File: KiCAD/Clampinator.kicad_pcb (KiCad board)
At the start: 4 copper layers, 200 x 130 mm, 194 parts, among them J1 Power, J10 Conn_01x04, J11 Conn_01x04, J12 FDCAN_1, J13 FDCAN_2, J14 10k NTC, J15 10k NTC, J16 EN_NTC_B, J17 EN_NTC_A, J18 FAN, J19 FAN, J20 VP0265840000G, J23 VP0265840000G, J24 VP0265840000G, J25 +5V INJ, J5 Debug Header, J6 Conn_01x04, J7 Conn_01x04, J8 Conn_01x04, J9 Conn_01x04, Q1 TK100E10N1,S1X, Q10 AO3400A, Q2 TK100E10N1,S1X, Q3 TK100E10N1,S1X, Q4 TK100E10N1,S1X, Q5 TK100E10N1,S1X, Q6 AO3400A, Q7 AO3400A, Q8 AO3400A, Q9 MMBT3904-C20526, SW1 PTS810SJM250SMTRLFS, SW2 PTS810SJM250SMTRLFS, SW3 PTS810SJM250SMTRLFS, SW4 PTS810SJM250SMTRLFS, SW5 SMQS-02R-TP, SW6 EG1847-ND, SW7 GPI-154-3013, U1 STM32H573RIT6, U10 LM74810QDRRRQ1, U12 TPS7A2033DQNR, U13 VOS618A-3T, U14 LM5163DDAR, U2 TL432BQDBZR, U3 EG2131, U4 UCC33420RAQR_C46461551, U5 USBLC6-2SC6, U6 LM5012DDAR, U7 MCP2562FD-E/P, U8 MCP2562FD-E/P, U9 EL357N, X1 SC-32S32.768kHz20PPM7pF, Y2 ECS-80-18-23B-JTM-TR

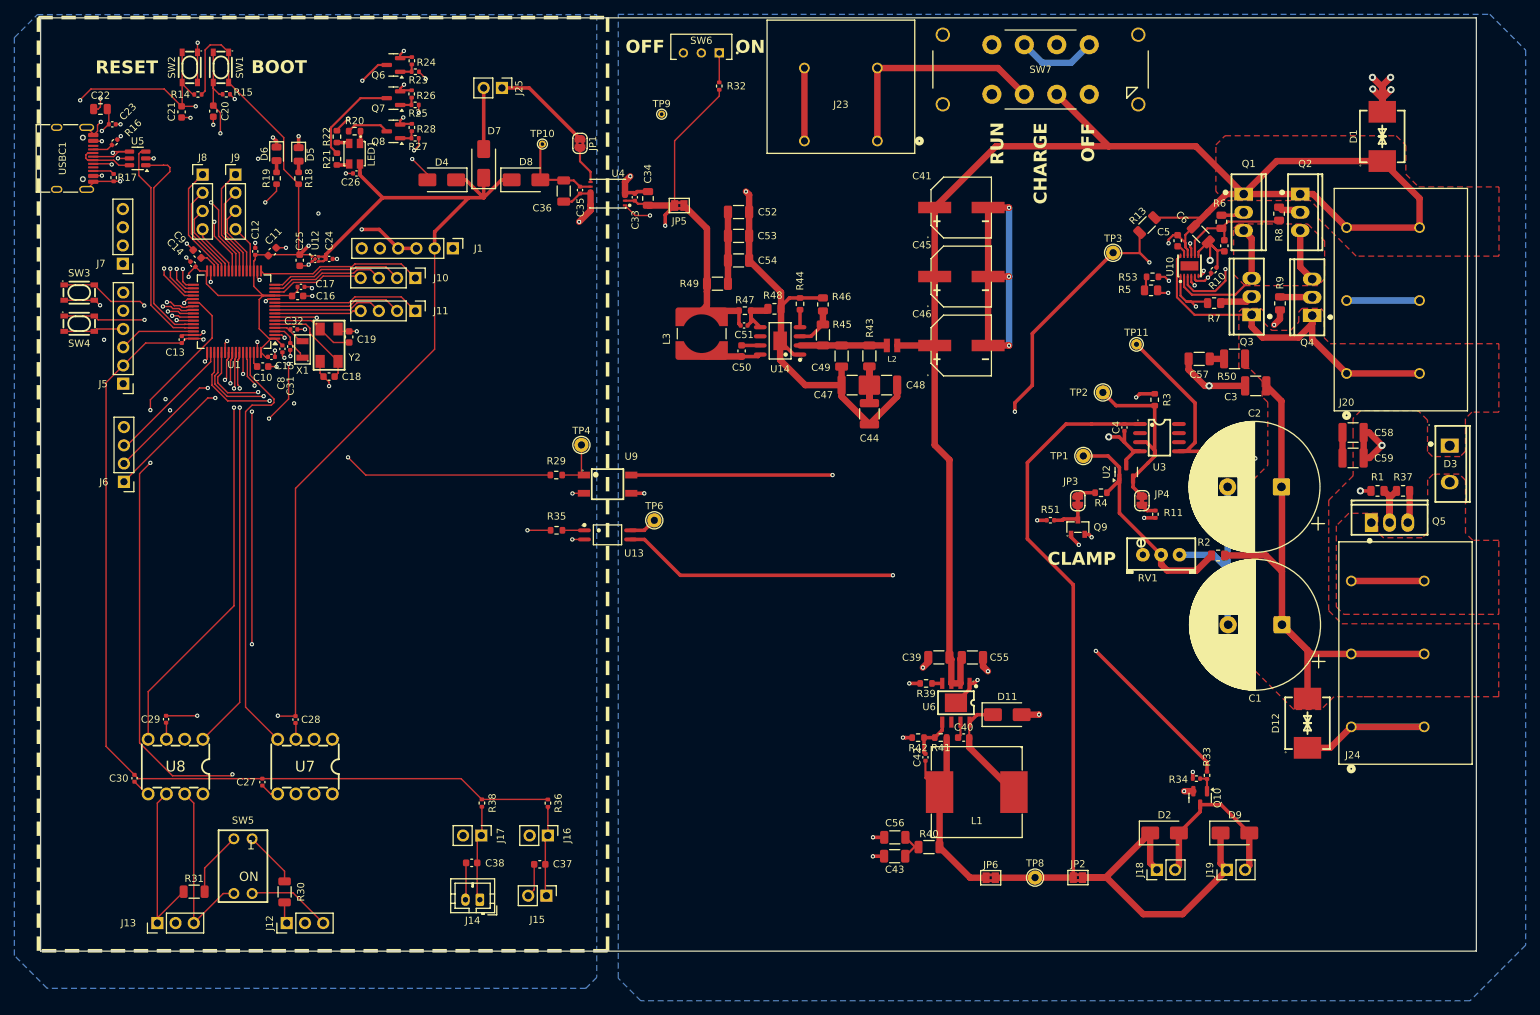
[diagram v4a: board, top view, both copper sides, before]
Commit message: Add full stack GND fills, adjust thermal spoke widths, silkscreen clearance/other DRC warning fixes
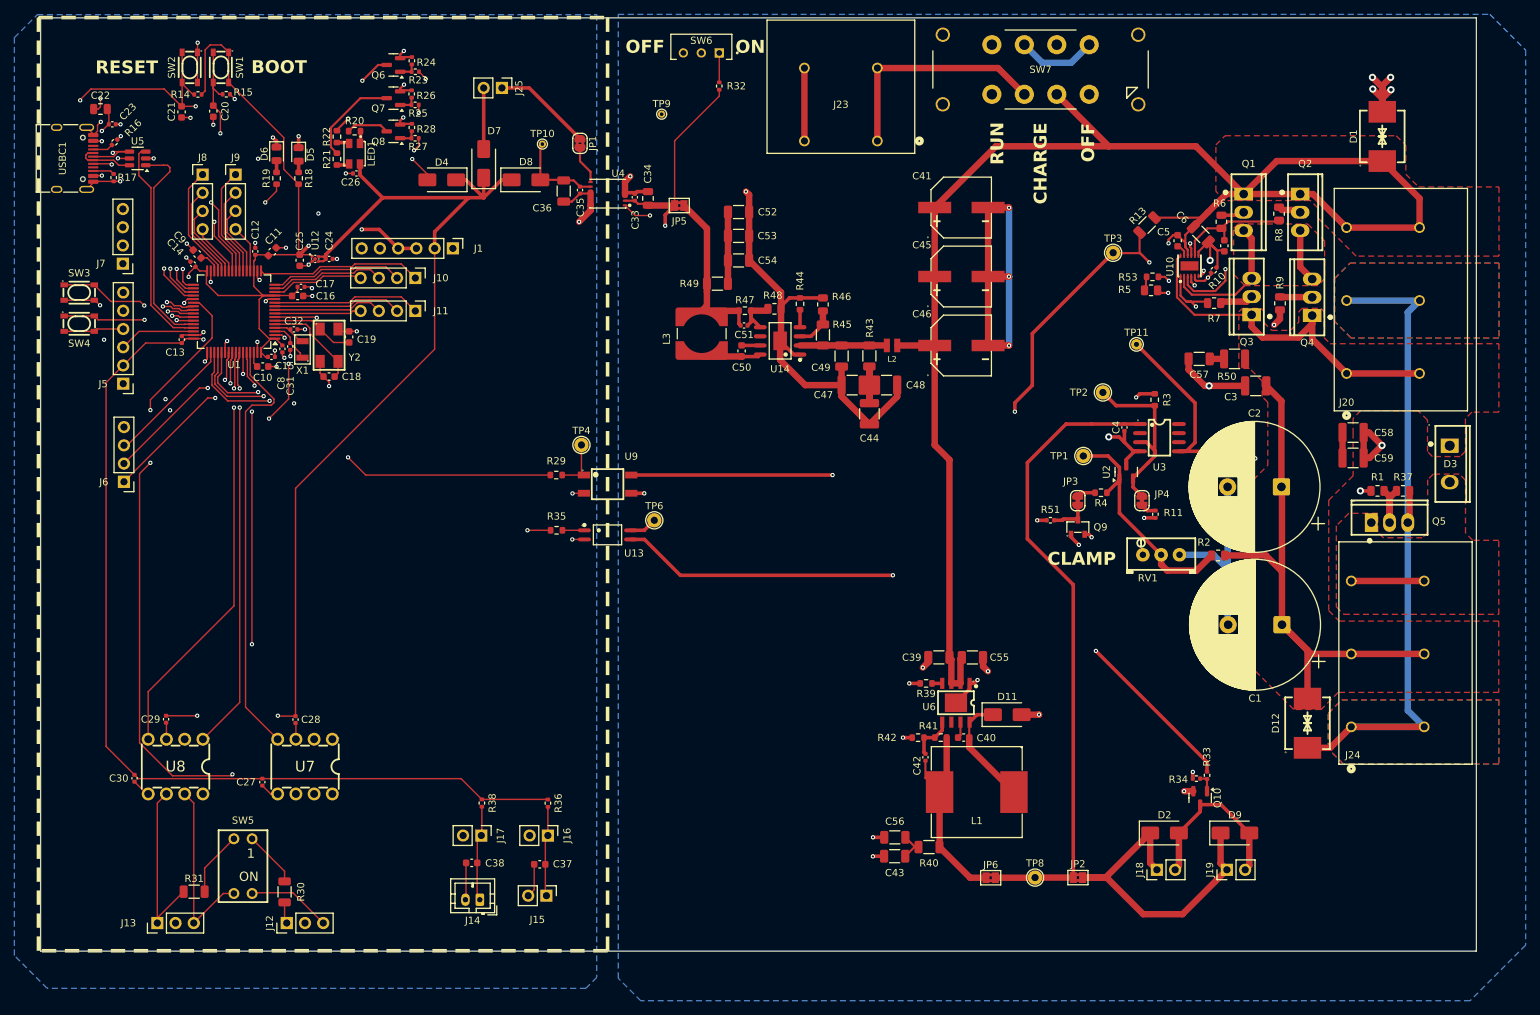
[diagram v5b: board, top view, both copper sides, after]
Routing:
- net DC_GND: track 276.1 -> 337.1 mm
- added copper zone on F.Cu, net DC_GND
- added copper zone on In1.Cu, net DC_GND
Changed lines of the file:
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@@
 		(tags "resistor")
 		(property "Reference" "R40"
-			(at 0 -1.83 0)
+			(at 0 2.24 0)
 			(layer "F.SilkS")
 			(effects
@@
 		(tags "capacitor")
 		(property "Reference" "C43"
-			(at 0 -1.85 0)
+			(at 0 -2.32 0)
 			(layer "F.SilkS")
 			(effects
@@
 		(tags "resistor")
 		(property "Reference" "R42"
-			(at 0 -1.43 0)
+			(at 4.325 -0.005777 0)
 			(layer "F.SilkS")
 			(effects
@@
 		(tags "capacitor")
 		(property "Reference" "C40"
-			(at 0 -1.43 0)
+			(at 3.155 0.055777 0)
 			(layer "F.SilkS")
 			(effects
@@
 		(tags "resistor")
 		(property "Reference" "R41"
-			(at 0 -1.43 0)
+			(at 1.715 1.614223 0)
 			(layer "F.SilkS")
 			(effects
@@
 		(tags "capacitor")
 		(property "Reference" "C42"
-			(at 0 -1.16 90)
+			(at -1.17 -1.16 90)
 			(layer "F.SilkS")
 			(effects
@@
 		)
 		(fp_text user "1"
-			(at -1.66 2.93 0)
+			(at -1.66 1.7672 0)
 			(layer "F.SilkS")
 			(effects
@@
 		(tags "capacitor")
 		(property "Reference" "C56"
-			(at 0 2.005 0)
+			(at 0 2.225 0)
 			(layer "F.SilkS")
 			(effects
@@
 	)
 	(segment
+		(start 238.2539 65.5407)
+		(end 239.8902 63.9044)
+		(width 0.9)
+		(layer "B.Cu")
+		(net "DC_GND")
+	)
+	(segment
 		(start 191.3592 30.7848)
 		(end 193.8758 28.2682)
@@
 	)
 	(segment
+		(start 238.2539 121.0075)
+		(end 240.538 123.2916)
+		(width 0.9)
+		(layer "B.Cu")
+		(net "DC_GND")
+	)
+	(segment
 		(start 229.7302 63.9044)
 		(end 239.8902 63.9044)
@@
 	)
 	(segment
+		(start 238.2539 94.8398)
+		(end 238.2539 121.0075)
+		(width 0.9)
+		(layer "B.Cu")
+		(net "DC_GND")
+	)
+	(segment
 		(start 182.71 50.98)
 		(end 182.71 60.55)
@@
 	)
 	(segment
+		(start 238.2539 94.8398)
+		(end 238.2539 65.5407)
+		(width 0.9)
+		(layer "B.Cu")
+		(net "DC_GND")
+	)
+	(segment
 		(start 213.15182 108.99342)
 		(end 213.226 109.0676)
@@
 	)
 	(zone
+		(net "DC_GND")
+		(layers "F.Cu" "B.Cu" "In1.Cu" "In2.Cu")
+		(hatch edge 0.5)
+		(priority 6)
+		(connect_pads yes
+			(clearance 0.8)
+		)
+		(min_thickness 0.25)
+		(fill yes
+			(thermal_gap 0.5)
+			(thermal_bridge_width 0.5)
+			(island_removal_mode 0)
+		)
+		(polygon
+			(pts
+				(xy 228.06 60.840002) (xy 230.210002 58.69) (xy 250.94 58.69) (xy 250.94 69.12) (xy 230.3625 69.12)
+				(xy 228.06 66.8175)
+			)
+		)
+	)
+	(zone
+		(net "DC_GND")
+		(layers "F.Cu" "B.Cu" "In1.Cu" "In2.Cu")
+		(hatch edge 0.5)
+		(priority 6)
+		(connect_pads yes
+			(clearance 0.8)
+		)
+		(min_thickness 0.25)
+		(fill yes
+			(thermal_gap 0.5)
+			(thermal_bridge_width 0.5)
+			(island_removal_mode 0)
+		)
+		(polygon
+			(pts
+				(xy 227.18 121.400002) (xy 229.060002 119.52) (xy 250.92 119.52) (xy 250.92 128.46) (xy 229.28 128.46)
+				(xy 227.18 126.36)
+			)
+		)
+	)
+	(zone
 		(net "DC_VIN")
 		(layers "F.Cu" "In1.Cu")
@@
 		(priority 4)
 		(connect_pads yes
-			(clearance 0.5)
+			(clearance 0.8)
 		)
 		(min_thickness 0.25)
@@
 		(priority 3)
 		(connect_pads yes
-			(clearance 0.5)
+			(clearance 0.8)
 		)
 		(min_thickness 0.25)
@@
 		(polygon
 			(pts
-				(xy 250.92 108.93) (xy 250.92 119.09) (xy 232.96 119.09) (xy 231.97 119.09) (xy 227.97 119.090072)
-				(xy 226.1914 120.8686) (xy 222.3686 120.8686) (xy 216.74 115.24) (xy 216.74 88.869557) (xy 218.75 86.857664)
-				(xy 218.75 78.070697) (xy 217.9684 77.3) (xy 217.9684 75.1184) (xy 216.2094 73.3594) (xy 214.72 73.3594)
-				(xy 214.72 65.479918) (xy 215.201132 64.99895) (xy 217.800782 65.000657) (xy 218.18 65.380123) (xy 218.18 66.95)
-				(xy 219.29 68.06) (xy 221.920002 68.06) (xy 223.07 66.910002) (xy 223.07 65.46) (xy 223.54 64.99)
-				(xy 226.142673 64.99) (xy 226.57 65.422582) (xy 226.57 69.05) (xy 227.44 69.92) (xy 246.53 69.92)
-				(xy 250.94 69.92) (xy 250.94 79.45) (xy 247.18 79.45) (xy 246.28 80.35) (xy 246.28 84.91) (xy 245.55 85.64)
-				(xy 241.69 85.64) (xy 241 84.95) (xy 241 80.56) (xy 239.70059 79.26059) (xy 231.694586 79.240878)
-				(xy 230.631737 80.304009) (xy 230.632 82.296) (xy 230.64 88.32) (xy 227.240698 91.72) (xy 227.24 95.52)
-				(xy 227.24 107.11) (xy 229.06 108.93) (xy 232.75 108.93)
+				(xy 250.92 108.56) (xy 250.92 118.489965) (xy 228.570061 118.490035) (xy 226.1914 120.8686) (xy 222.3686 120.8686)
+				(xy 216.74 115.24) (xy 216.74 88.869557) (xy 218.75 86.857664) (xy 218.75 78.070697) (xy 217.9684 77.3)
+				(xy 217.9684 75.1184) (xy 216.2094 73.3594) (xy 214.72 73.3594) (xy 214.72 65.479918) (xy 215.201132 64.99895)
+				(xy 217.800782 65.000657) (xy 218.18 65.380123) (xy 218.18 66.95) (xy 219.29 68.06) (xy 221.920002 68.06)
+				(xy 223.07 66.910002) (xy 223.07 65.46) (xy 223.54 64.99) (xy 226.142673 64.99) (xy 226.57 65.422582)
+				(xy 226.57 69.05) (xy 227.44 69.92) (xy 246.53 69.92) (xy 250.94 69.92) (xy 250.94 79.45) (xy 247.18 79.45)
+				(xy 246.28 80.35) (xy 246.28 84.91) (xy 245.55 85.64) (xy 241.69 85.64) (xy 241 84.95) (xy 241 80.56)
+				(xy 239.70059 79.26059) (xy 231.694586 79.240878) (xy 230.631737 80.304009) (xy 230.632 82.296)
+				(xy 230.64 88.32) (xy 227.240698 91.72) (xy 227.24 95.52) (xy 227.24 107.11) (xy 228.69 108.56)
 			)
 		)
@@
 		(priority 5)
 		(connect_pads yes
-			(clearance 0.5)
+			(clearance 0.8)
 		)
 		(min_thickness 0.25)
@@
 		(priority 2)
 		(connect_pads yes
-			(clearance 0.5)
+			(clearance 0.8)
 		)
 		(min_thickness 0.25)
@@
 		(fill yes
 			(thermal_gap 0.5)
-			(thermal_bridge_width 0.5)
+			(thermal_bridge_width 1.25)
 			(island_removal_mode 0)
 		)

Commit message: Oscillator Test Pads + Re-Fix USB-C
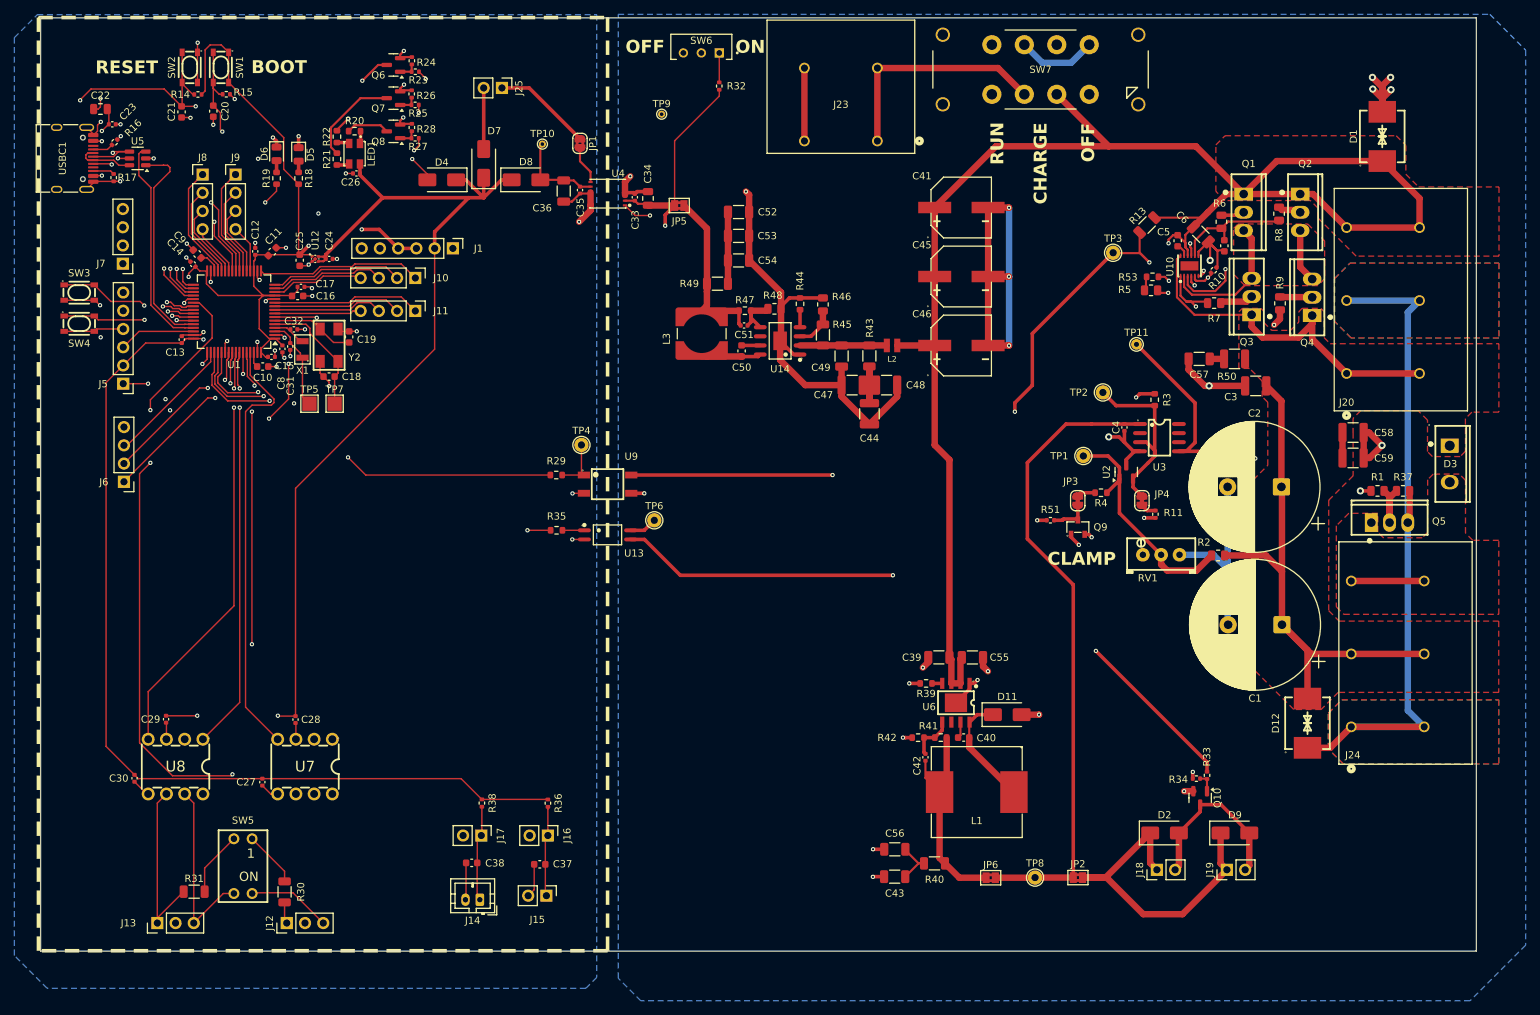
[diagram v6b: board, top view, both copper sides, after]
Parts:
- added TP5: LSE, TestPoint:TestPoint_Pad_2.0x2.0mm, F.Cu at (85.3, 78.3)
- added TP7: HSE, TestPoint:TestPoint_Pad_2.0x2.0mm, F.Cu at (88.8, 78.3)
- moved C43 2.85 mm to (166.8, 144.2)
- moved R40 2.40 mm to (172.3, 142.3)
- moved C56 1.66 mm to (166.8, 140.3)
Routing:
- net LSE_IN: track 6.04 -> 12.8 mm
- net HSE_IN: track 13.7 -> 17.5 mm
- net PC9: track 44.5 -> 41.0 mm
- net +3V3: track 253.3 -> 251.6 mm
- net Net-(C43-Pad1): track 4.75 -> 6.09 mm
- net CAN2_STBY: track 86.4 -> 87.4 mm
- net Net-(JP6-A): track 29.1 -> 30.0 mm
- net SWO: vias 1 -> 2

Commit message: Shrunk edge cuts, Started fixing GND fills, Changed pad shapes, Nudged footprints around
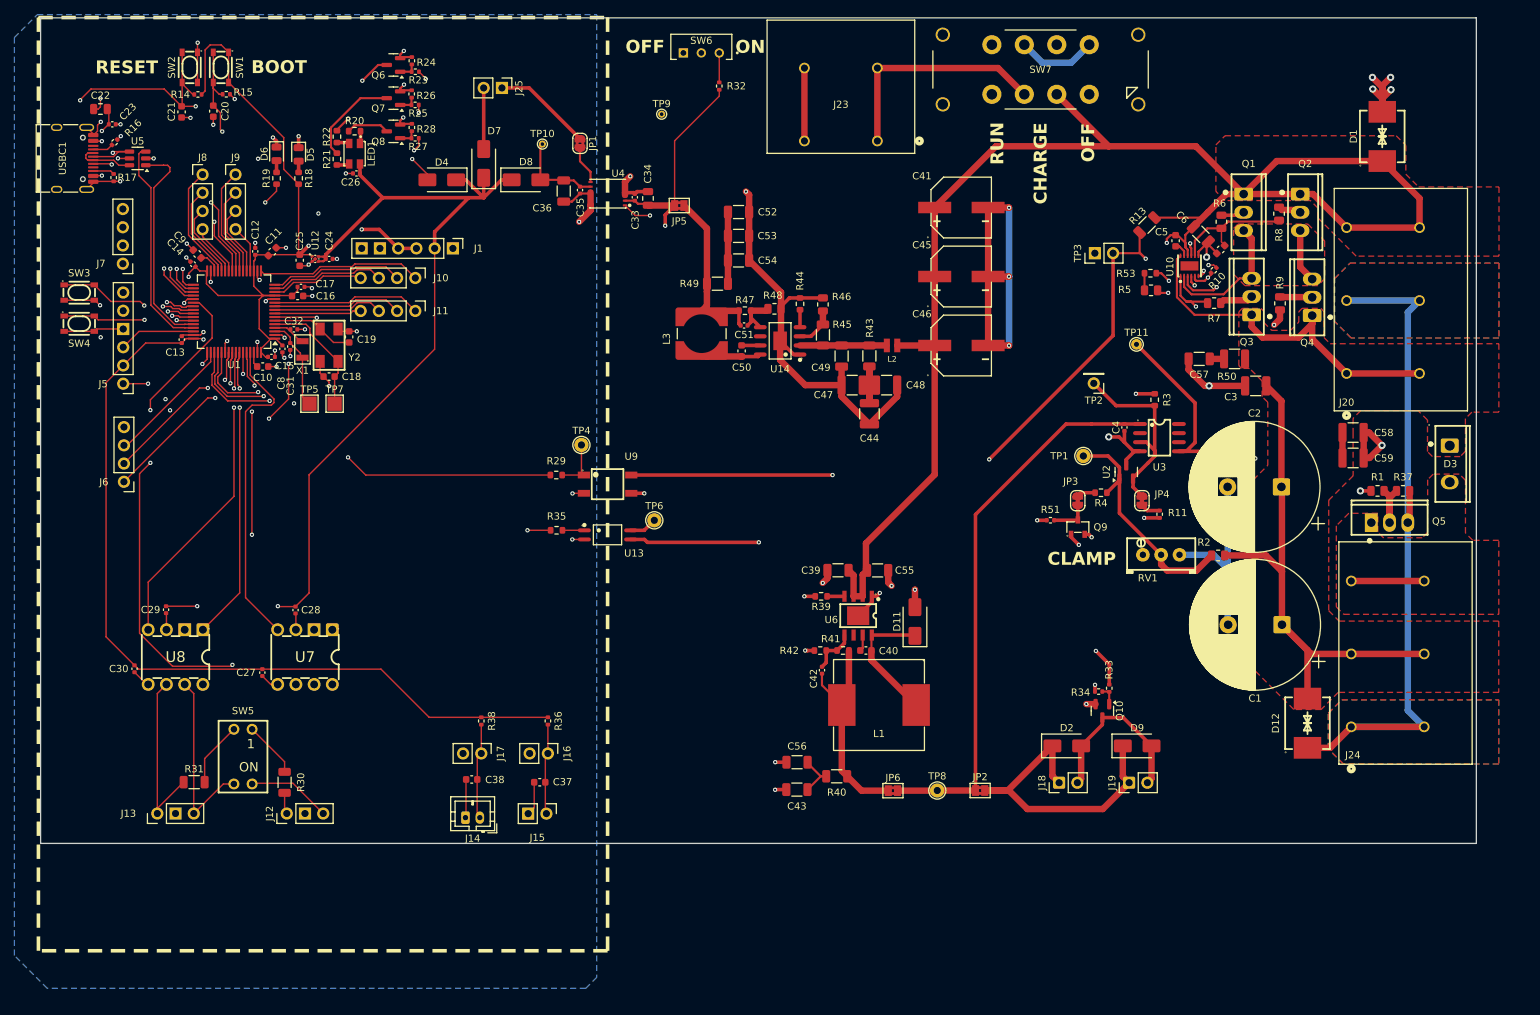
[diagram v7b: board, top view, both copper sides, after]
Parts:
- TP2: footprint TestPoint:TestPoint_THTPad_D2.0mm_Drill1.0mm -> Connector_PinHeader_2.54mm:PinHeader_1x01_P2.54mm_Vertical
- TP3: footprint TestPoint:TestPoint_THTPad_D2.0mm_Drill1.0mm -> Connector_PinHeader_2.54mm:PinHeader_1x02_P2.54mm_Vertical
- moved R39 19.0 mm to (156.5, 105.1)
- moved C42 18.8 mm to (156.7, 115.4)
- moved C39 18.6 mm to (158.9, 101.5)
- moved D11 18.3 mm to (169.6, 108.6), turned to 90 degrees
- moved U6 18.2 mm to (161.7, 107.8)
- moved C40 18.2 mm to (162.8, 112.7)
- moved C43 18.2 mm to (153.2, 132.0)
- moved D2 18.2 mm to (190.7, 125.9)
- moved D9 18.2 mm to (200.6, 125.9)
- moved J18 18.2 mm to (189.7, 131.1)
- moved J19 18.2 mm to (199.4, 131.1)
- moved JP2 18.2 mm to (178.7, 132.2)
- moved JP6 18.2 mm to (166.5, 132.2)
- moved L1 18.2 mm to (164.6, 120.2)
- moved Q10 18.2 mm to (195.7, 121.1)
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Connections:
- TP3 pad 1: EN_DIODE -> DC_GND
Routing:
- net Net-(R33-Pad2): track 94.5 -> 76.7 mm
- net FDCAN2_TX: track 56.2 -> 41.0 mm
- net FDCAN1_TX: track 59.0 -> 43.8 mm
- net FDCAN1_RX: track 60.3 -> 45.1 mm
- net CAN2_STBY: track 87.4 -> 72.1 mm
- net CAN1_STBY: track 97.0 -> 81.8 mm
- net FDCAN2_RX: track 58.9 -> 43.7 mm
- net +5VS: track 147.1 -> 131.8 mm
- net +3V3: track 251.6 -> 238.0 mm
- net +15VR: track 89.2 -> 77.4 mm
- net NTC_A_IN: track 119.5 -> 108.1 mm
- net DC_VIN: track 267.3 -> 258.2 mm
- net NTC_B_IN: track 116.8 -> 110.0 mm
- net EN_DIODE: track 146.3 -> 143.0 mm
- net DC_GND: track 337.1 -> 334.0 mm, vias 25 -> 26
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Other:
- board size 200 x 130 mm -> 200 x 115 mm
